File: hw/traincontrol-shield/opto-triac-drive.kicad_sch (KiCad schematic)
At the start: 6 parts, among them U5 MOC3021M, U6 MOC3021M

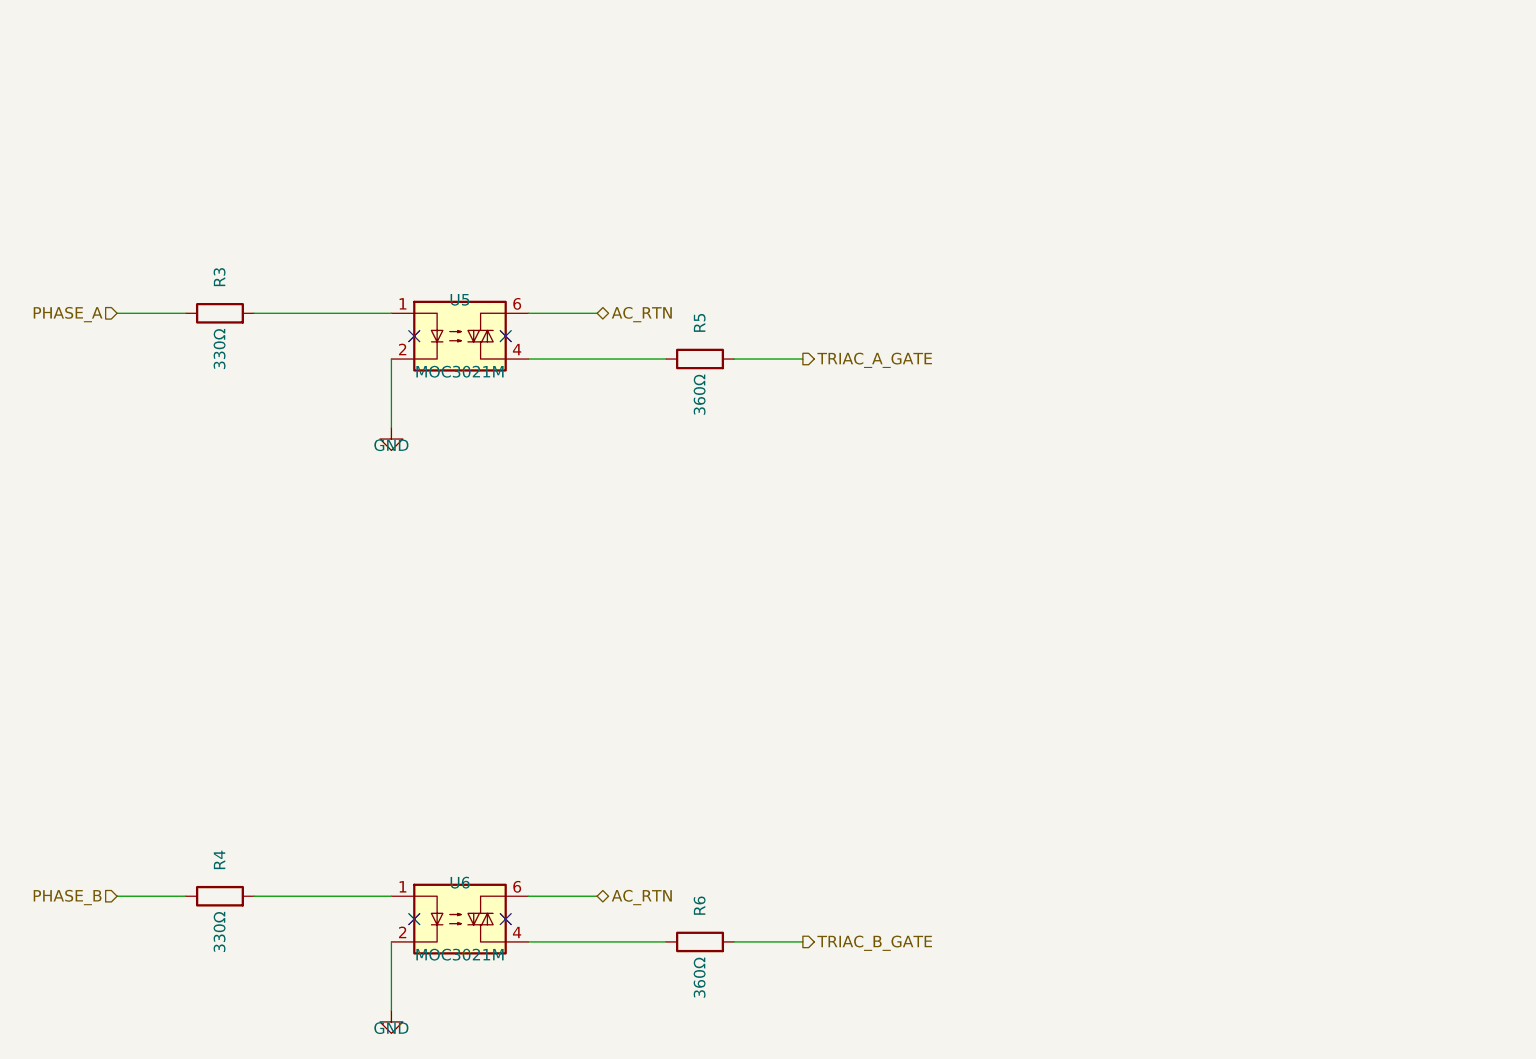
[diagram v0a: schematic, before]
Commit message: Schematic updates by hand.
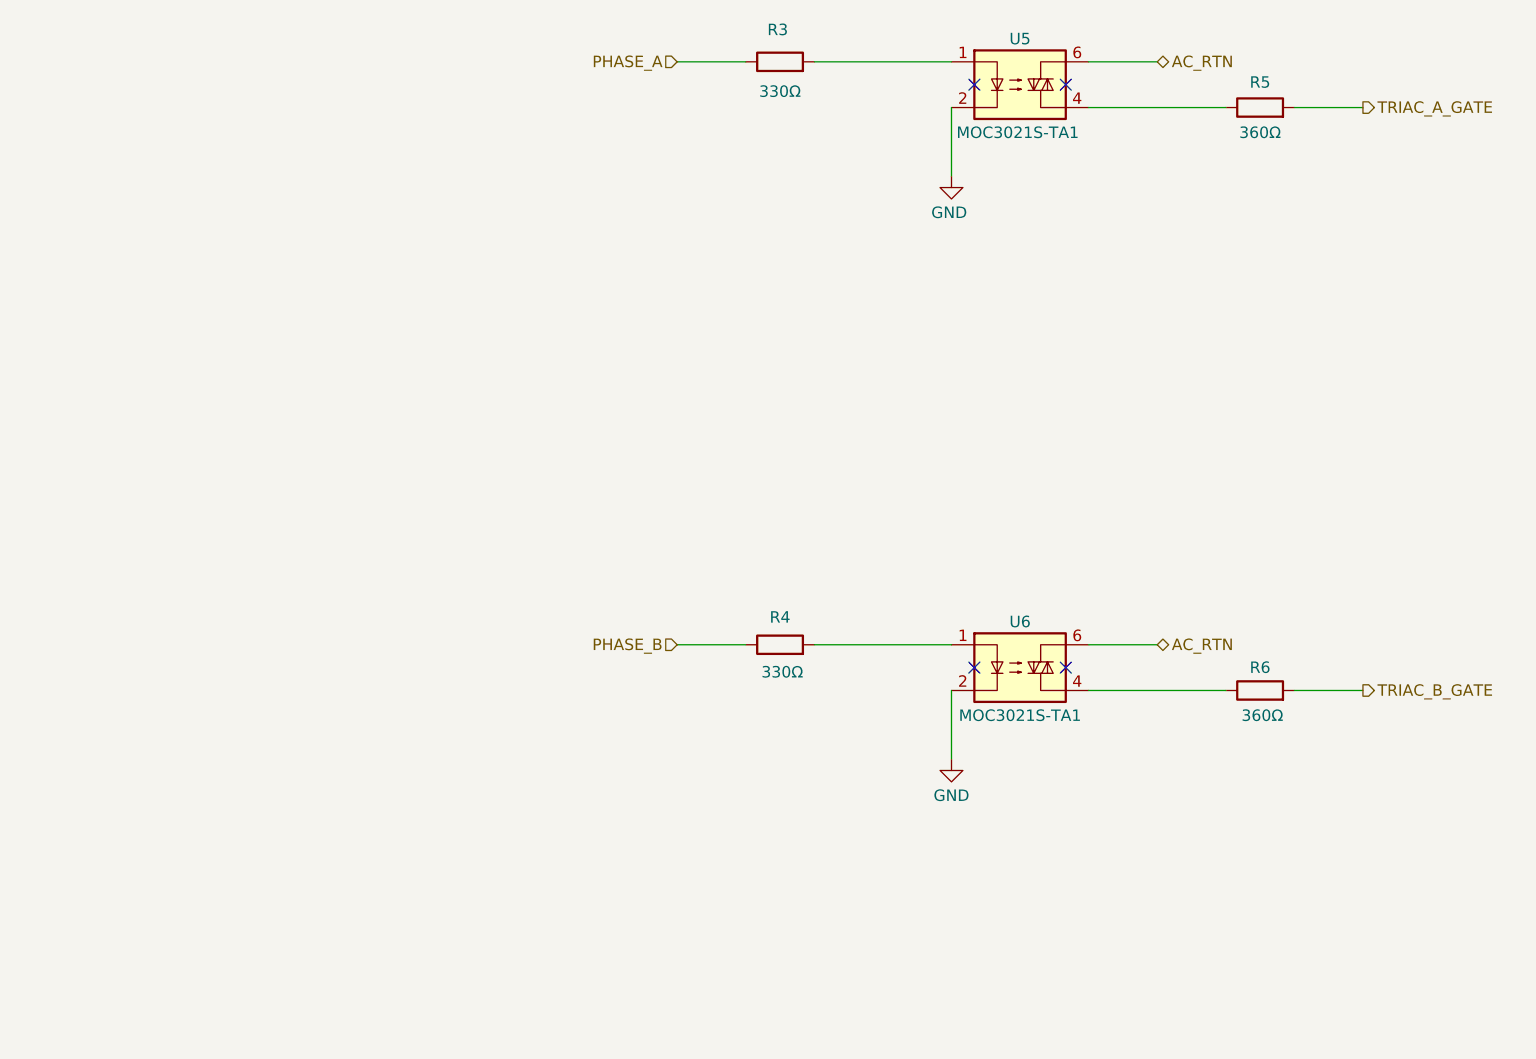
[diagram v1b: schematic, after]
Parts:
- U5, U6: value MOC3021M -> MOC3021S-TA1; footprint Package_DIP:DIP-6_W7.62mm -> traincontrol-shield:SMD-6_L7.3-W6.5-P2.54-LS10.2-BL; LCSC Part (none) -> C115465
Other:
- moved on the sheet: R3, R4, R5, R6, U5, U6
